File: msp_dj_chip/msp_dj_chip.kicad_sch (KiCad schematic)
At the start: 86 parts, among them J1 Conn_01x04_Pin, J10 Conn_01x02_Socket, J11 Conn_01x02_Socket, J12 Conn_01x02_Socket, J13 Conn_01x02_Socket, J14 Conn_01x02_Socket, J15 Conn_01x02_Socket, J16 Conn_01x02_Socket, J17 Conn_01x02_Socket, J18 Conn_01x02_Socket, J19 Conn_01x02_Socket, J2 Conn_01x04_Pin, J20 Conn_01x02_Socket, J21 Conn_01x02_Socket, J22 Conn_01x06_Socket, J23 Conn_01x06_Socket, J3 Conn_01x02_Socket, J4 Conn_01x02_Socket, J5 Conn_01x02_Socket, J6 Conn_01x02_Socket, J8 Conn_02x05_Odd_Even, J9 Conn_01x02_Socket, U2 DAC60502, U4 NCP1117-3.3_SOT223, U8 NCV272DMR2G, Y2 Crystal_GND24_Small

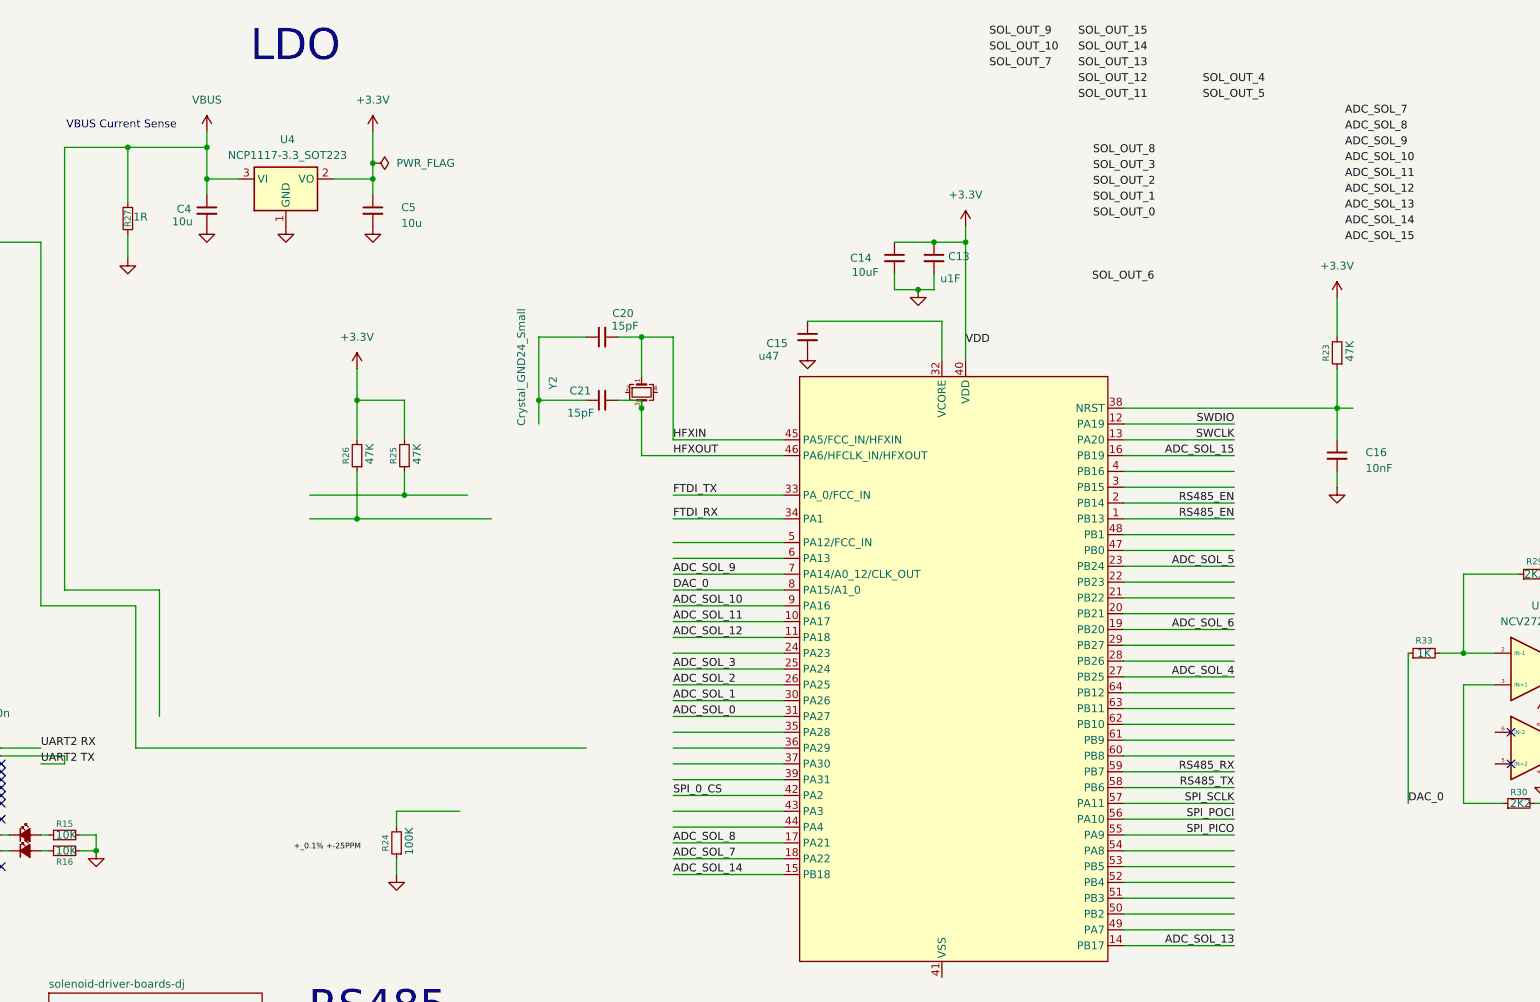
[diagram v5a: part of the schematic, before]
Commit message: adding back footprints and symbols
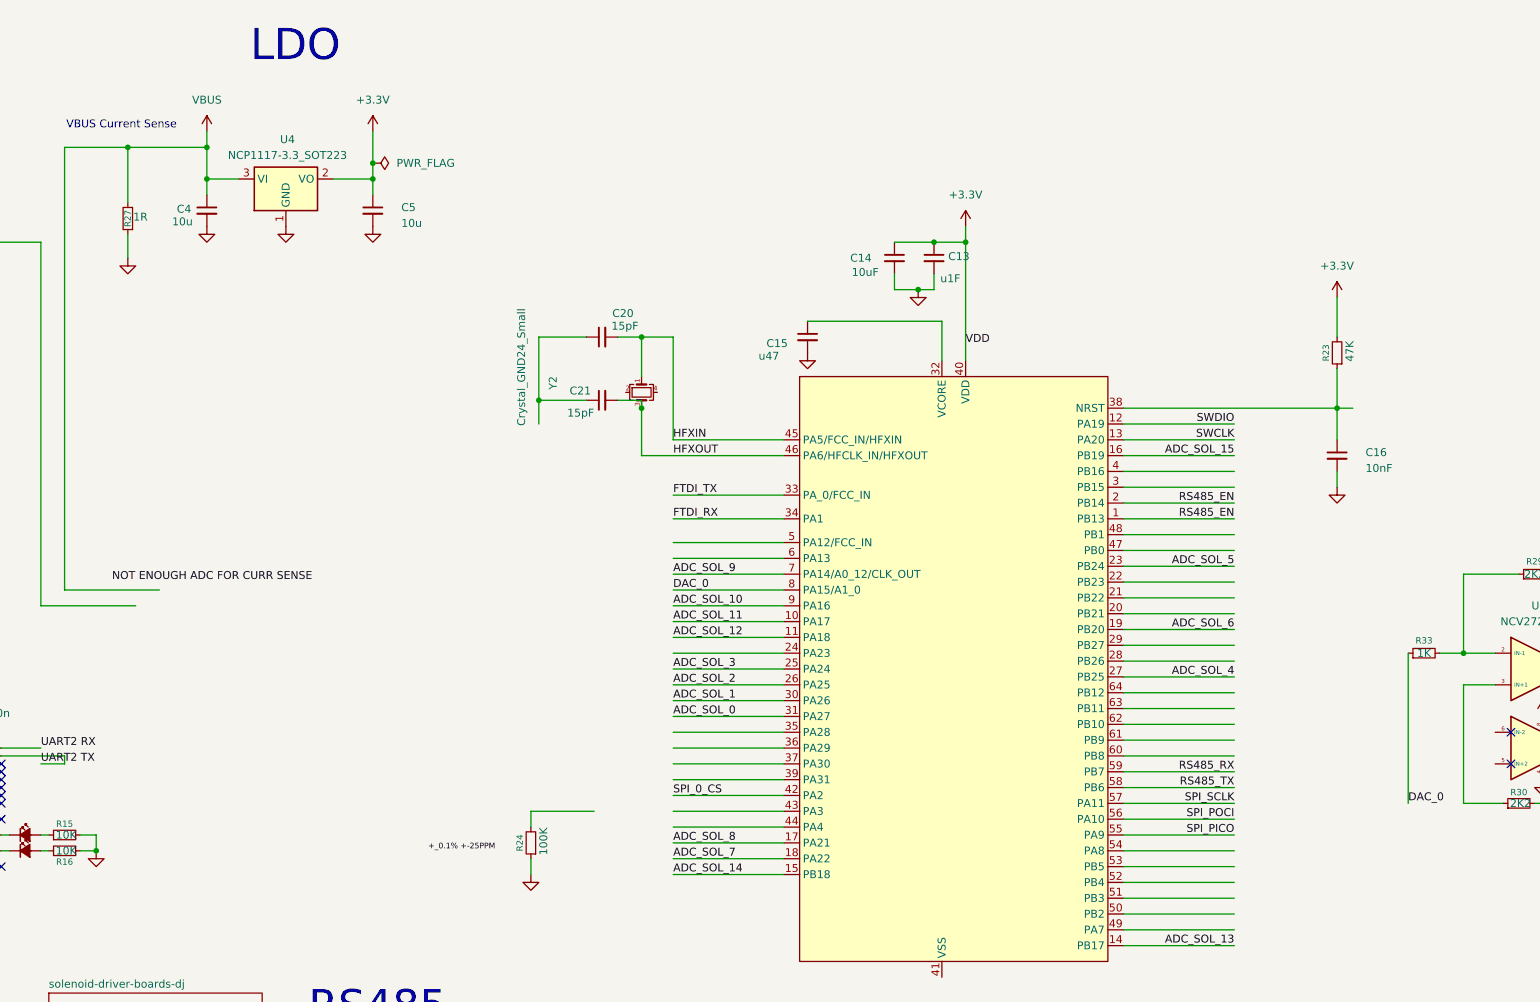
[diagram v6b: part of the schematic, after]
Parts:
- removed R25, R26: 47K, symbol Device:R_Small
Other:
- moved on the sheet: R24

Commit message: labeled sol pins on mcu
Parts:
- added SW1: SW_MEC_5E, symbol Switch:SW_MEC_5E
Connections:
- net GND: now also C20.1, C21.1, Y2.2, Y2.4, SW1.3 (K), SW1.4 (A)
- net at C16.1, R23.1, U6.38 (NRST): now also SW1.1, SW1.2
- net GPIO_SOL_04: now reaches U6.20 (PB21)
- net GPIO_SOL_05: now reaches U6.21 (PB22)
- net GPIO_SOL_06: now reaches U6.22 (PB23)
- net GPIO_SOL_07: now reaches U6.24 (PA23)
- net GPIO_SOL_08: now reaches U6.28 (PB26)
- net GPIO_SOL_09: now reaches U6.29 (PB27)
- net GPIO_SOL_00: now reaches U6.3 (PB15)
- net GPIO_SOL_10: now reaches U6.35 (PA28)
- net GPIO_SOL_11: now reaches U6.36 (PA29)
- net GPIO_SOL_12: now reaches U6.37 (PA30)
- net GPIO_SOL_13: now reaches U6.39 (PA31)
- net GPIO_SOL_01: now reaches U6.4 (PB16)
- net GPIO_SOL_14: now reaches U6.43 (PA3)
- net GPIO_SOL_15: now reaches U6.44 (PA4)
- net GPIO_SOL_02: now reaches U6.5 (PA12/FCC_IN)
- net GPIO_SOL_03: now reaches U6.6 (PA13)
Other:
- moved on the sheet: C1, C10, C11, C12, C13, C14, C15, C16, C2, C20, C21, C3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

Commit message: some changes
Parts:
- added F1, F2: Fuse_Small, symbol Device:Fuse_Small
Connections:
- net +24V: now also F1.2, F2.2
- net OUT_0: now also F2.1
- net OUT_1: now also F1.1
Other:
- sheet solenoid-driver-boards-dj ports: added GPIO_INPUT_00, GPIO_INPUT_01, OUT_00, OUT_01; removed none
